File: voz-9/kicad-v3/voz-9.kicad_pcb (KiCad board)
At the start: 2 copper layers, 200 x 100 mm, 199 parts, among them J1 fio 20, J2 fio 12, J3 fio 20, J4 fio 20, J5 fio 16, J6 fio 6, J7 fio 12, J8 fio 6, J9 fio 12, Q1 MMBFJ201, Q2 MMBFJ201, Q3 MMBFJ201, Q4 MMBFJ201, Q5 MMBFJ201, Q6 MMBFJ201, Q7 MMBF5457, U1 NE5532DR, U2 TL072CDR, U3 TL072CDR, U4 ICL7660, U5 78M05, U6 PT2399, U7 PT2399, U8 PT2399, U9 TL072CDR

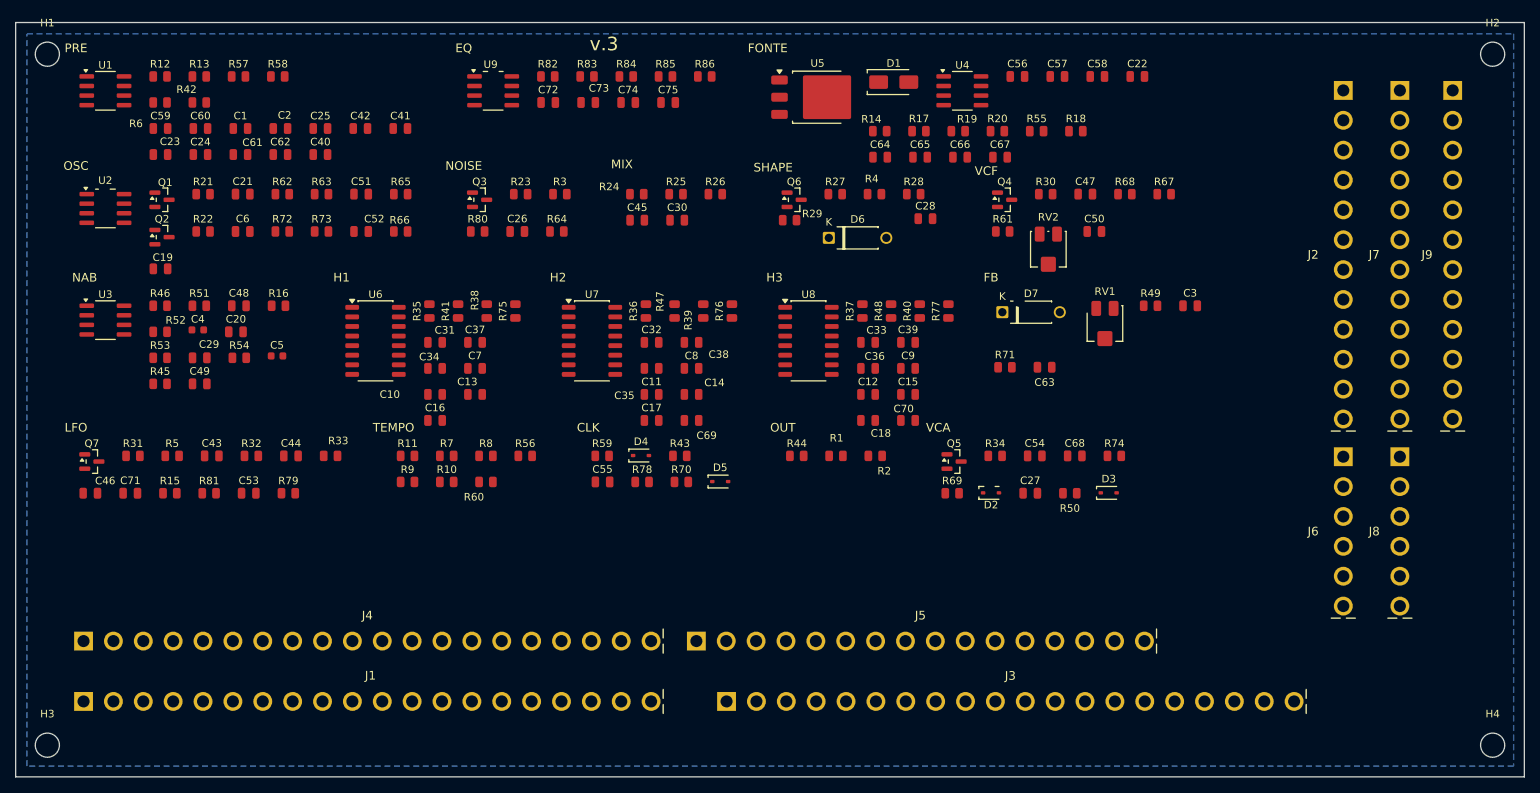
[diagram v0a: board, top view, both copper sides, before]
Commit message: Agrupa os furos da v3 por controle da interface.
Cada pot, chave e jack vira um footprint separado, com o mesmo número de pino. O primeiro furo do grupo fica quadrado.

Co-authored-by: Andrey <andreysenes@users.noreply.github.com>
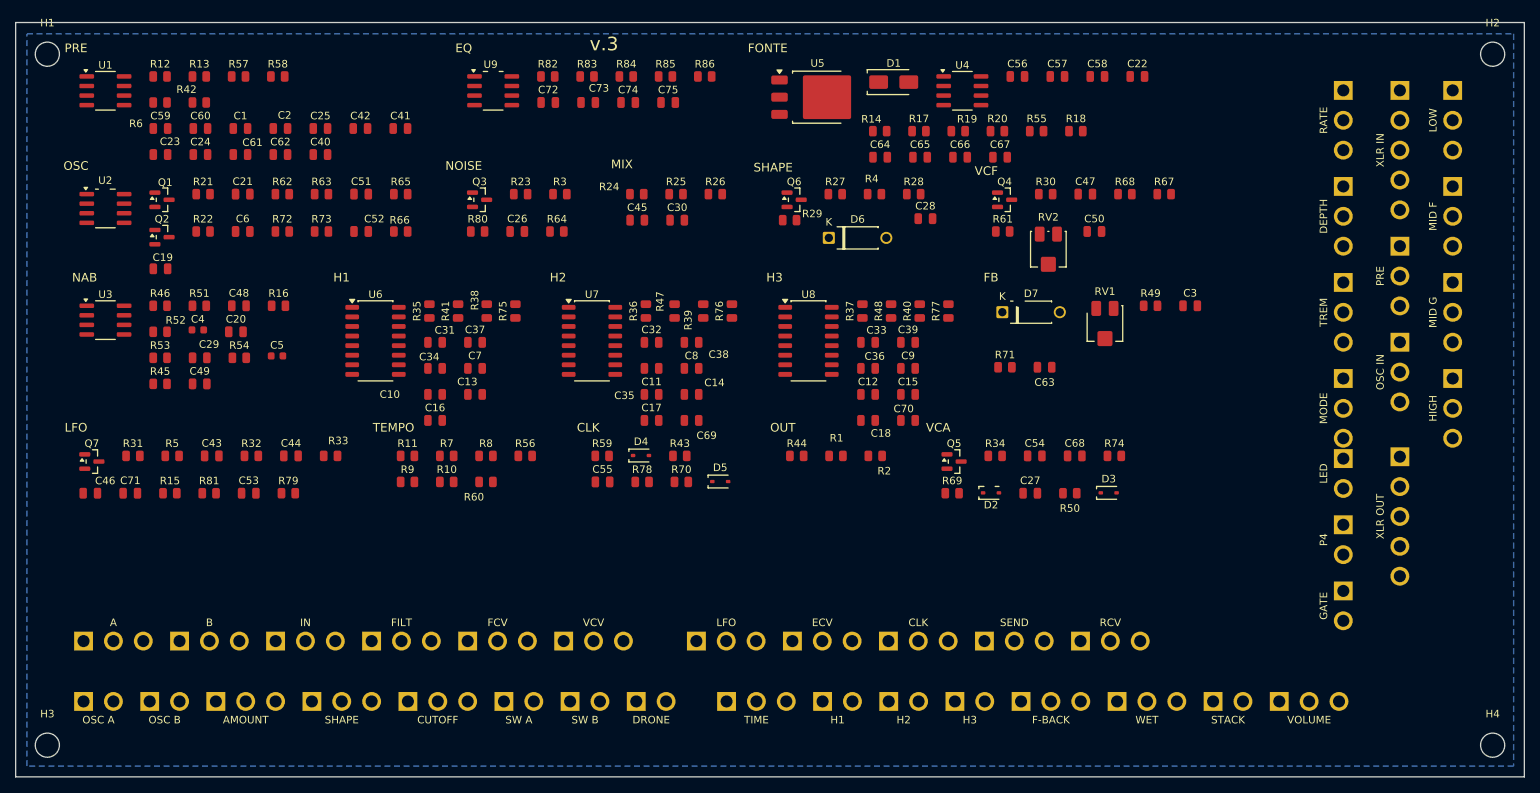
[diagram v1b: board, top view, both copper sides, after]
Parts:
- removed the J1 at (9.00, 90.0)
- removed the J2 at (176.0, 9.00)
- removed the J3 at (94.2, 90.0)
- removed the J4 at (9.00, 82.0)
- removed the J5 at (90.2, 82.0)
- removed the J6 at (176.0, 57.6)
- removed the J7 at (183.5, 9.00)
- removed the J9 at (190.5, 9.00)
- added J1: CUTOFF, , F.Cu at (52.0, 90.0)
- added J1: OSC A, , F.Cu at (9.00, 90.0)
- added J1: SHAPE, , F.Cu at (39.3, 90.0)
- added J1: SW B, , F.Cu at (73.5, 90.0)
- added J1: DRONE, , F.Cu at (82.3, 90.0)
- added J1: AMOUNT, , F.Cu at (26.5, 90.0)
- added J1: SW A, , F.Cu at (64.7, 90.0)
- added J1: OSC B, , F.Cu at (17.8, 90.0)
- added J2: MODE, , F.Cu at (176.0, 47.2)
- added J2: RATE, , F.Cu at (176.0, 9.00)
- added J2: DEPTH, , F.Cu at (176.0, 21.7)
- added J2: TREM, , F.Cu at (176.0, 34.5)
- added J3: H1, , F.Cu at (107.0, 90.0)
- added J3: WET, , F.Cu at (146.0, 90.0)
- added J3: H2, , F.Cu at (115.7, 90.0)
- added J3: STACK, , F.Cu at (158.7, 90.0)
- added J3: H3, , F.Cu at (124.5, 90.0)
- added J3: TIME, , F.Cu at (94.2, 90.0)
- added J3: F-BACK, , F.Cu at (133.3, 90.0)
- added J3: VOLUME, , F.Cu at (167.5, 90.0)
- added J4: VCV, , F.Cu at (72.7, 82.0)
- added J4: A, , F.Cu at (9.00, 82.0)
- added J4: IN, , F.Cu at (34.5, 82.0)
- added J4: FILT, , F.Cu at (47.2, 82.0)
- added J4: FCV, , F.Cu at (59.9, 82.0)
- added J4: B, , F.Cu at (21.7, 82.0)
- added J5: CLK, , F.Cu at (115.7, 82.0)
- added J5: RCV, , F.Cu at (141.2, 82.0)
- added J5: LFO, , F.Cu at (90.2, 82.0)
- added J5: SEND, , F.Cu at (128.4, 82.0)
- added J5: ECV, , F.Cu at (103.0, 82.0)
- added J6: LED, , F.Cu at (176.0, 57.8)
- added J6: GATE, , F.Cu at (176.0, 75.3)
- added J6: P4, , F.Cu at (176.0, 66.6)
- added J7: XLR IN, , F.Cu at (183.5, 9.00)
- added J7: PRE, , F.Cu at (183.5, 29.6)
- added J7: OSC IN, , F.Cu at (183.5, 42.4)
- added J9: MID G, , F.Cu at (190.5, 34.5)
- added J9: LOW, , F.Cu at (190.5, 9.00)
- added J9: HIGH, , F.Cu at (190.5, 47.2)
- added J9: MID F, , F.Cu at (190.5, 21.7)
- J8: value fio 6 -> XLR OUT; footprint VOZ9_Wire:WirePin_1x06_P3.96mm_D1.6mm -> (none)
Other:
- board text removed: "J1"
- board text removed: "J2"
- board text removed: "J3"
- board text removed: "J4"
- board text removed: "J5"
- board text removed: "J6"
- board text removed: "J7"
- board text removed: "J8"
- board text removed: "J9"

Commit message: Leva os pinos da interface da v3 para a base da placa.
Quatro linhas, passo de 3,96 mm e um vão do mesmo passo entre controles. O nome de cada grupo fica embaixo dos furos.

Co-authored-by: Andrey <andreysenes@users.noreply.github.com>
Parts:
- moved J9 97.4 mm to (119.8, 76.0), turned to 90 degrees
- moved J7 89.8 mm to (115.8, 68.0), turned to 90 degrees
- moved J2 89.2 mm to (127.7, 84.0), turned to 90 degrees
- moved J3 77.6 mm to (16.8, 84.0)
- moved J9 77.2 mm to (135.6, 76.0), turned to 90 degrees
- moved J3 74.5 mm to (32.7, 84.0)
- moved J3 71.4 mm to (44.6, 84.0)
- moved J2 70.2 mm to (143.6, 84.0), turned to 90 degrees
- moved J3 68.3 mm to (56.4, 84.0)
- moved J3 65.2 mm to (68.3, 84.0)
- moved J3 62.1 mm to (84.2, 84.0)
- moved J6 59.2 mm to (127.7, 92.0), turned to 90 degrees
- moved J3 59.0 mm to (100.0, 84.0)
- moved J7 58.3 mm to (139.6, 68.0), turned to 90 degrees
- moved J9 57.0 mm to (151.5, 76.0), turned to 90 degrees
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
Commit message: Ordena os pinos da interface da v3 pelo caminho do som.
XLR IN fica ao lado de XLR OUT, OSC A ao lado de OSC B, e as quatro linhas seguem entrada, vozes, timbre e fita até o VOLUME.

Co-authored-by: Andrey <andreysenes@users.noreply.github.com>
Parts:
- moved J2 111.2 mm to (64.4, 92.0)
- moved J2 111.2 mm to (16.8, 92.0)
- moved J2 111.2 mm to (32.7, 92.0)
- moved J2 111.2 mm to (48.5, 92.0)
- moved J5 108.1 mm to (159.4, 84.0)
- moved J5 108.1 mm to (143.6, 84.0)
- moved J5 108.1 mm to (175.2, 84.0)
- moved J8 105.7 mm to (60.4, 68.0)
- moved J9 103.3 mm to (16.8, 84.0)
- moved J9 103.3 mm to (64.4, 84.0)
- moved J9 103.3 mm to (48.5, 84.0)
- moved J9 103.3 mm to (32.7, 84.0)
- moved J7 79.2 mm to (36.6, 68.0)
- moved J3 75.7 mm to (159.4, 92.0)
- moved J3 75.7 mm to (143.6, 92.0)
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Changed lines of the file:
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@@
 	(footprint ""
 		(layer "F.Cu")
-		(at 76.24 92)
+		(at 96.04 84)
 		(property "Reference" "J1"
 			(at 0 0 0)
@@
 	(footprint ""
 		(layer "F.Cu")
-		(at 68.32 68)
+		(at 175.24 84)
 		(property "Reference" "J5"
 			(at 0 0 0)
@@
 		)
 		(property "Value" "CLK"
-			(at 3.959999 2.45 0)
+			(at 3.96 2.45 0)
 			(layer "F.SilkS")
 			(effects
@@
 	(footprint ""
 		(layer "F.Cu")
-		(at 32.68 84)
+		(at 96.04 92)
 		(property "Reference" "J3"
 			(at 0 0 0)
@@
 	(footprint ""
 		(layer "F.Cu")
-		(at 20.8 92)
+		(at 28.72 76)
 		(property "Reference" "J1"
 			(at 0 0 0)
@@
 	(footprint ""
 		(layer "F.Cu")
-		(at 115.84 68 90)
+		(at 36.64 68 90)
 		(property "Reference" "J7"
 			(at 0 0 0)
@@
 	(footprint ""
 		(layer "F.Cu")
-		(at 60.4 92)
+		(at 80.2 84)
 		(property "Reference" "J1"
 			(at 0 0 0)
@@
 	(footprint ""
 		(layer "F.Cu")
-		(at 84.16 84)
+		(at 159.4 92)
 		(property "Reference" "J3"
 			(at 0 0 0)
@@
 	(footprint ""
 		(layer "F.Cu")
-		(at 175.24 84 90)
+		(at 64.36 92 90)
 		(property "Reference" "J2"
 			(at 0 0 0)
@@
 	(footprint ""
 		(layer "F.Cu")
-		(at 163.36 92 90)
+		(at 60.4 68 90)
 		(property "Reference" "J8"
 			(at 0 0 0)
@@
 		)
 		(property "Value" "XLR OUT"
-			(at -2.45 7.919999 0)
+			(at -2.45 7.92 0)
 			(layer "F.SilkS")
 			(effects
@@
 	(footprint ""
 		(layer "F.Cu")
-		(at 100 68)
+		(at 131.68 68)
 		(property "Reference" "J5"
 			(at 0 0 0)
@@
 	(footprint ""
 		(layer "F.Cu")
-		(at 103.96 92)
+		(at 64.36 76)
 		(property "Reference" "J1"
 			(at 0 0 0)
@@
 	(footprint ""
 		(layer "F.Cu")
-		(at 127.72 84 90)
+		(at 16.84 92 90)
 		(property "Reference" "J2"
 			(at 0 0 0)
@@
 	(footprint ""
 		(layer "F.Cu")
-		(at 103.96 76)
+		(at 163.36 76)
 		(property "Reference" "J4"
 			(at 0 0 0)
@@
 	(footprint ""
 		(layer "F.Cu")
-		(at 127.72 92 90)
+		(at 147.52 68 90)
 		(property "Reference" "J6"
 			(at 0 0 0)
@@
 		)
 		(property "Value" "LED"
-			(at -2.45 1.979999 0)
+			(at -2.45 1.98 0)
 			(layer "F.SilkS")
 			(effects
@@
 	(footprint ""
 		(layer "F.Cu")
-		(at 44.56 84)
+		(at 107.92 92)
 		(property "Reference" "J3"
 			(at 0 0 0)
@@
 	(footprint ""
 		(layer "F.Cu")
-		(at 151.48 76 90)
+		(at 48.52 84 90)
 		(property "Reference" "J9"
 			(at 0 0 0)
@@
 	(footprint ""
 		(layer "F.Cu")
-		(at 36.639999 68)
+		(at 143.56 84)
 		(property "Reference" "J5"
 			(at 0 0 0)
@@
 	(footprint ""
 		(layer "F.Cu")
-		(at 143.56 84 90)
+		(at 32.68 92 90)
 		(property "Reference" "J2"
 			(at 0 0 0)
@@
 	(footprint ""
 		(layer "F.Cu")
-		(at 100 84)
+		(at 131.68 92)
 		(property "Reference" "J3"
 			(at 0 0 0)
@@
 	(footprint ""
 		(layer "F.Cu")
-		(at 24.76 76)
+		(at 76.24 76)
 		(property "Reference" "J4"
 			(at 0 0 0)
@@
 	(footprint ""
 		(layer "F.Cu")
-		(at 56.44 76)
+		(at 123.76 76)
 		(property "Reference" "J4"
 			(at 0 0 0)
@@
 	(footprint ""
 		(layer "F.Cu")
-		(at 151.48 92 90)
+		(at 151.48 76 90)
 		(property "Reference" "J6"
 			(at 0 0 0)
@@
 		)
 		(property "Value" "GATE"
-			(at -2.45 1.979999 0)
+			(at -2.45 1.98 0)
 			(layer "F.SilkS")
 			(effects
@@
 	(footprint ""
 		(layer "F.Cu")
-		(at 119.8 76 90)
+		(at 16.84 84 90)
 		(property "Reference" "J9"
 			(at 0 0 0)
@@
 	(footprint ""
 		(layer "F.Cu")
-		(at 139.6 68 90)
+		(at 84.16 68 90)
 		(property "Reference" "J7"
 			(at 0 0 0)
@@
 		)
 		(property "Value" "PRE"
-			(at -2.45 3.96 0)
+			(at -2.45 3.959999 0)
 			(layer "F.SilkS")
 			(effects
@@
 	(footprint ""
 		(layer "F.Cu")
-		(at 56.44 84)
+		(at 119.8 92)
 		(property "Reference" "J3"
 			(at 0 0 0)
@@
 	(footprint ""
 		(layer "F.Cu")
-		(at 167.32 76 90)
+		(at 64.36 84 90)
 		(property "Reference" "J9"
 			(at 0 0 0)
@@
 	(footprint ""
 		(layer "F.Cu")
-		(at 115.84 92)
+		(at 139.6 76)
 		(property "Reference" "J1"
 			(at 0 0 0)
@@
 	(footprint ""
 		(layer "F.Cu")
-		(at 16.84 84)
+		(at 80.2 92)
 		(property "Reference" "J3"
 			(at 0 0 0)
@@
 	(footprint ""
 		(layer "F.Cu")
-		(at 84.16 68)
+		(at 115.84 68)
 		(property "Reference" "J5"
 			(at 0 0 0)
@@
 		)
 		(property "Value" "SEND"
-			(at 3.959999 2.45 0)
+			(at 3.96 2.45 0)
 			(layer "F.SilkS")
 			(effects
@@
 	(footprint ""
 		(layer "F.Cu")
-		(at 44.56 92)
+		(at 107.92 76)
 		(property "Reference" "J1"
 			(at 0 0 0)
@@
 	(footprint ""
 		(layer "F.Cu")
-		(at 139.6 92 90)
+		(at 159.4 68 90)
 		(property "Reference" "J6"
 			(at 0 0 0)
@@
 		)
 		(property "Value" "P4"
-			(at -2.45 1.979999 0)
+			(at -2.45 1.98 0)
 			(layer "F.SilkS")
 			(effects
@@
 	(footprint ""
 		(layer "F.Cu")
-		(at 52.479999 68)
+		(at 159.4 84)
 		(property "Reference" "J5"
 			(at 0 0 0)
@@
 	(footprint ""
 		(layer "F.Cu")
-		(at 135.64 76 90)
+		(at 32.68 84 90)
 		(property "Reference" "J9"
 			(at 0 0 0)
@@
 	(footprint ""
 		(layer "F.Cu")
-		(at 68.32 84)
+		(at 143.56 92)
 		(property "Reference" "J3"
 			(at 0 0 0)
@@
 	(footprint ""
 		(layer "F.Cu")
-		(at 155.44 68 90)
+		(at 100 68 90)
 		(property "Reference" "J7"
 			(at 0 0 0)
@@
 	(footprint ""
 		(layer "F.Cu")
-		(at 72.28 76)
+		(at 111.88 84)
 		(property "Reference" "J4"
 			(at 0 0 0)
@@
 	(footprint ""
 		(layer "F.Cu")
-		(at 92.08 92)
+		(at 52.48 76)
 		(property "Reference" "J1"
 			(at 0 0 0)
@@
 	(footprint ""
 		(layer "F.Cu")
-		(at 32.68 92)
+		(at 40.6 76)
 		(property "Reference" "J1"
 			(at 0 0 0)
@@
 	(footprint ""
 		(layer "F.Cu")
-		(at 88.12 76)
+		(at 127.72 84)
 		(property "Reference" "J4"
 			(at 0 0 0)
@@
 	(footprint ""
 		(layer "F.Cu")
-		(at 111.88 84)
+		(at 175.239999 92)
 		(property "Reference" "J3"
 			(at 0 0 0)
@@
 		)
 		(property "Value" "VOLUME"
-			(at 3.96 2.45 0)
+			(at 3.960001 2.45 0)
 			(layer "F.SilkS")
 			(effects
@@
 	(footprint ""
 		(layer "F.Cu")
-		(at 159.4 84 90)
+		(at 48.52 92 90)
 		(property "Reference" "J2"
 			(at 0 0 0)
@@
 	(footprint ""
 		(layer "F.Cu")
-		(at 40.6 76)
+		(at 92.08 76)
 		(property "Reference" "J4"
 			(at 0 0 0)

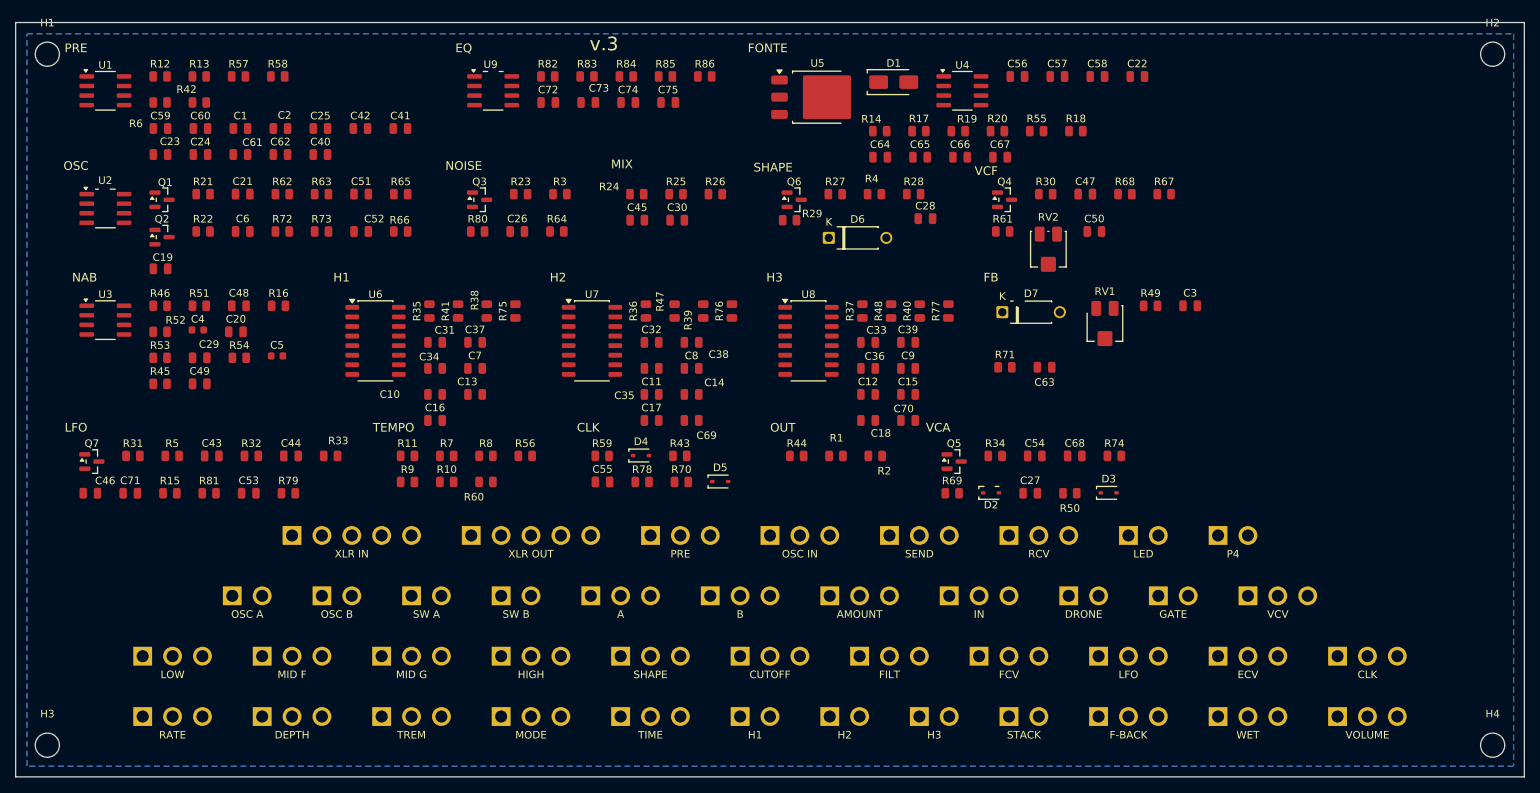
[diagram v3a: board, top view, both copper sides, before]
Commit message: Empilha LFO, TEMPO, CLK, OUT e VCA ao lado da fonte.
Os cinco blocos ficam numa coluna na área livre da direita, de cima para baixo, na ordem do sinal.

Co-authored-by: Andrey <andreysenes@users.noreply.github.com>
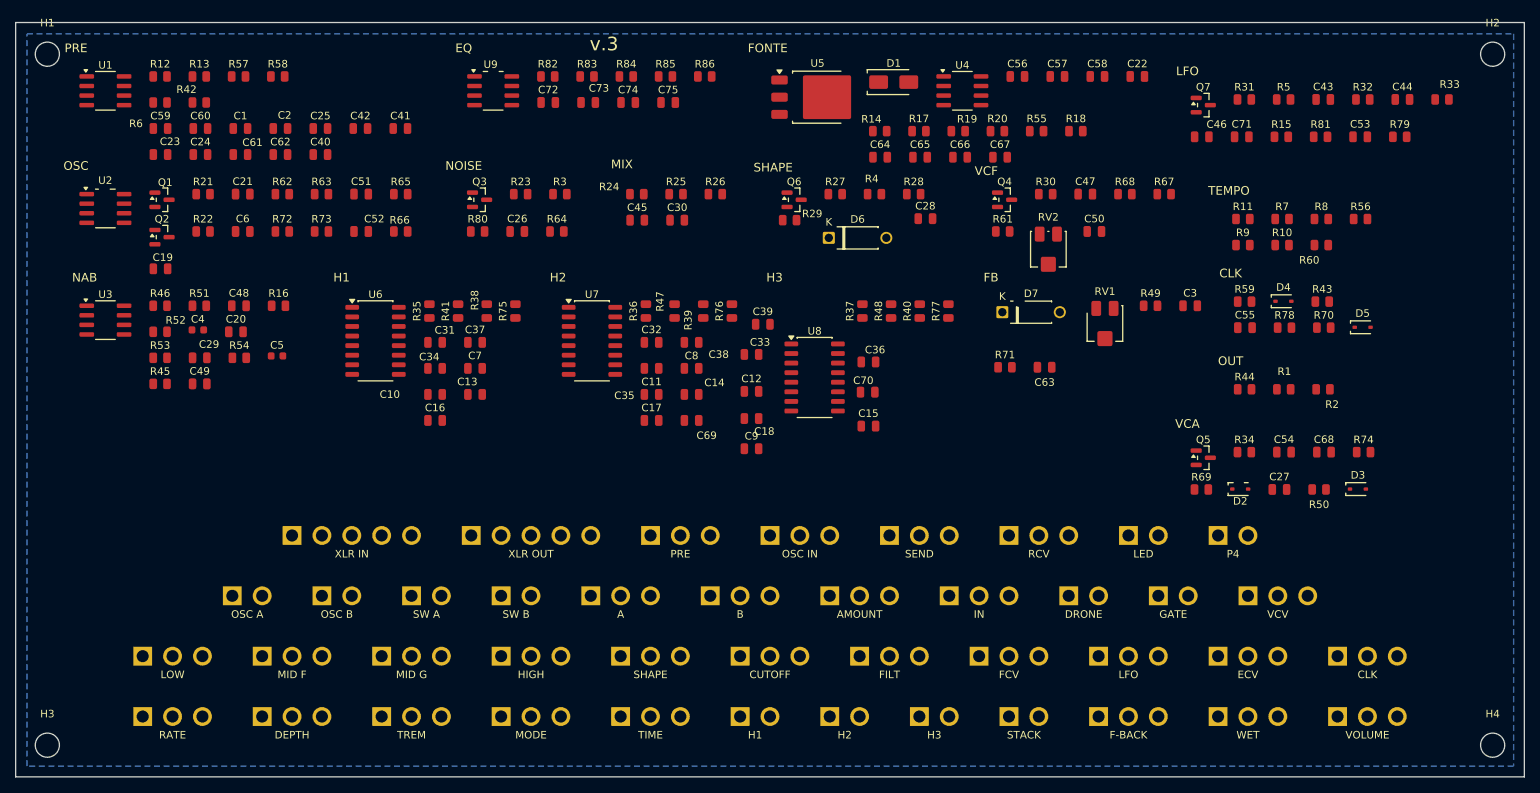
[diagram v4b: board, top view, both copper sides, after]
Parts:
- moved C43 154.7 mm to (173.3, 10.2)
- moved C44 154.7 mm to (183.8, 10.2)
- moved C46 154.7 mm to (157.2, 15.2)
- moved C53 154.7 mm to (178.2, 15.2)
- moved C71 154.7 mm to (162.5, 15.2)
- moved Q7 154.7 mm to (157.4, 10.9)
- moved R15 154.7 mm to (167.8, 15.2)
- moved R32 154.7 mm to (178.6, 10.2)
- moved R33 154.7 mm to (189.1, 10.2)
- moved R5 154.7 mm to (168.1, 10.2)
- moved R79 154.7 mm to (183.5, 15.2)
- moved R81 154.7 mm to (173.0, 15.2)
- moved R31 154.7 mm to (162.9, 10.2)
- moved R60 115.1 mm to (173.1, 29.5)
- moved R8 115.1 mm to (173.1, 26.1)
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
